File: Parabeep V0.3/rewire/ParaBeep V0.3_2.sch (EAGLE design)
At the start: 64 parts, among them IC2 MCP73811/2, Q1 500mA/300V, U1 ADXL345, U2 TPS78330DDCRDDC5_TEX-L, U3 TPS78330DDCRDDC5_TEX-L, U4 UBLOX_SAM_M8Q-0-10, U5 MS5803-14BA, U6 ATSAMD51J20A-A, U7 AT25SF128A-SHB-T, U8 RN4871-V/RM118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

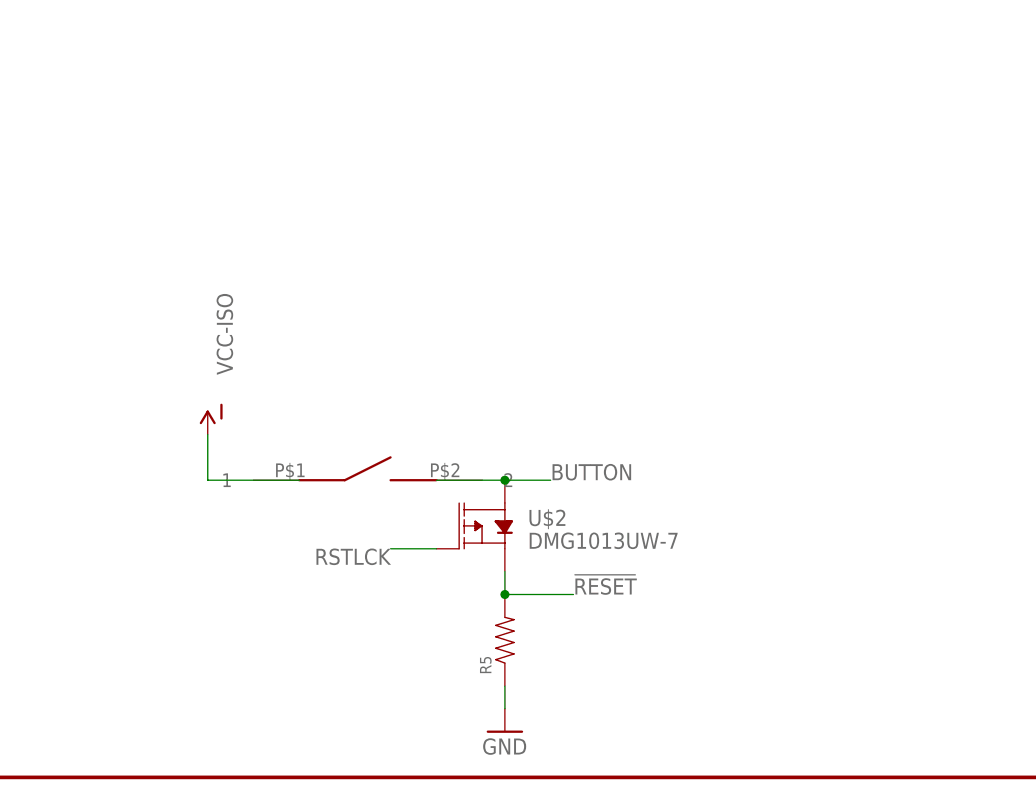
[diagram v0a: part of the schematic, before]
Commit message: bluetooth working, usb next
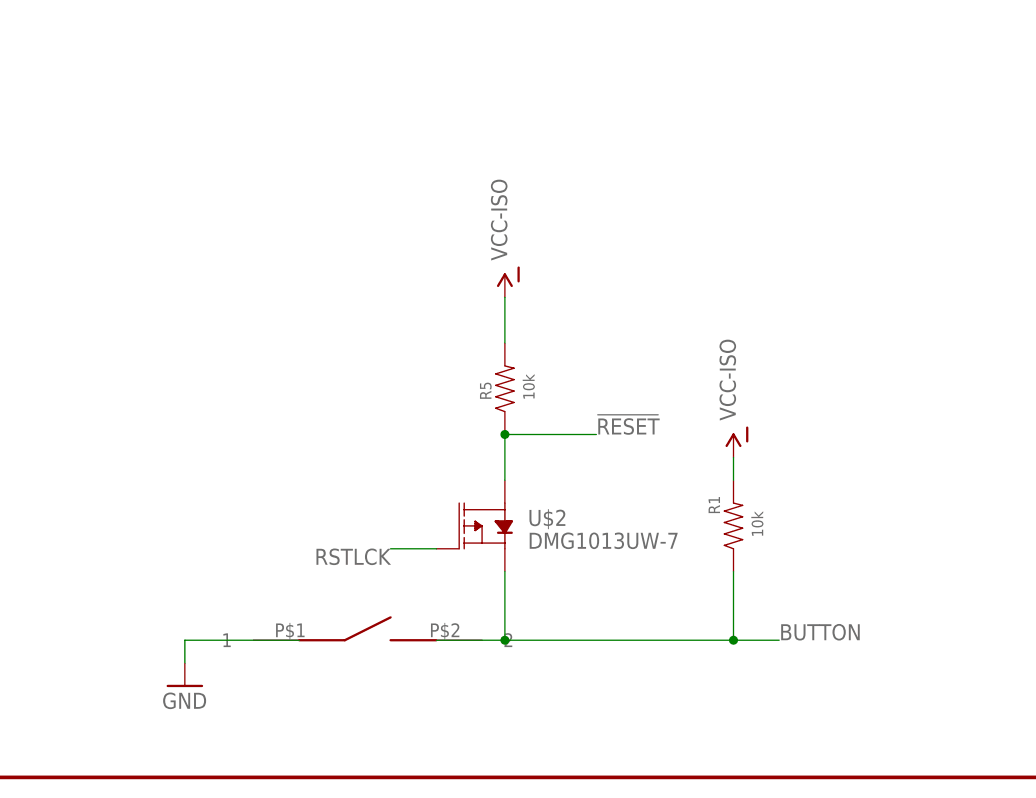
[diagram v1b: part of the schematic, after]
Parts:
- added R1: 10k, SparkFun-Resistors:RESISTOR0402
- R5: value (none) -> 10k
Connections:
- net !RESET: now also R5.1, U$2.S; no longer R5.2, U$2.D
- net BUTTON: now also R1.1, U$2.D; no longer U$2.S
- net GND: now also U$3.1; no longer R5.1
- net VCC-ISO: now also R1.2, R5.2; no longer U$3.1
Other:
- moved on the sheet: R5
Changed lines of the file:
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@@
 <part name="C12" library="SparkFun-Capacitors" deviceset="0.1UF" device="-0603-25V-(+80/-20%)" value="10uF"/>
 <part name="L2" library="SparkFun-Coils" deviceset="INDUCTOR" device="FB-30OHM"/>
-<part name="R5" library="SparkFun-Resistors" deviceset="RESISTOR" device="0402" value=" "/>
+<part name="R5" library="SparkFun-Resistors" deviceset="RESISTOR" device="0402" value="10k"/>
 <part name="GND4" library="SparkFun-Aesthetics" deviceset="GND" device=""/>
 <part name="SUPPLY10" library="SparkFun-PowerSymbols" deviceset="VCC_1" device=""/>
@@
 <part name="R12" library="SparkFun-Resistors" deviceset="RESISTOR" device="0402" value=" "/>
 <part name="GND23" library="SparkFun-Aesthetics" deviceset="GND" device=""/>
-<part name="U$6" library="SparkFun-PowerSymbols" deviceset="VCC-ISO" device=""/>
 <part name="J1" library="SparkFun-Connectors" deviceset="CONN_02" device="-JST-2MM-SMT"/>
 <part name="J3" library="SparkFun-Connectors" deviceset="CONN_02" device="-JST-2MM-SMT"/>
@@
 <part name="R6" library="SparkFun-Resistors" deviceset="RESISTOR" device="0402" value="100k"/>
 <part name="JP1" library="SparkFun-Jumpers" deviceset="JUMPER-SMT_3_1-NC_TRACE" device="_SILK" package3d_urn="urn:adsk.eagle:package:39288/1"/>
+<part name="U$6" library="SparkFun-PowerSymbols" deviceset="VCC-ISO" device=""/>
+<part name="R1" library="SparkFun-Resistors" deviceset="RESISTOR" device="0402" value="10k"/>
+<part name="U$8" library="SparkFun-PowerSymbols" deviceset="VCC-ISO" device=""/>
 </parts>
 <sheets>
@@
 <attribute name="VALUE" x="259.08" y="218.44" size="1.778" layer="96"/>
 </instance>
-<instance part="U$3" gate="G$1" x="254" y="33.02" smashed="yes"/>
+<instance part="U$3" gate="G$1" x="254" y="15.24" smashed="yes"/>
 <instance part="SUPPLY1" gate="G$1" x="25.4" y="259.08" smashed="yes">
 <attribute name="VALUE" x="25.4" y="261.874" size="1.778" layer="96" rot="MR0" align="bottom-center"/>
@@
 <attribute name="VALUE" x="73.66" y="184.15" size="1.778" layer="96" font="vector" rot="R90" align="top-left"/>
 </instance>
-<instance part="R5" gate="G$1" x="269.24" y="15.24" smashed="yes" rot="R90">
-<attribute name="NAME" x="267.7414" y="11.43" size="1.27" layer="95" rot="R90"/>
-<attribute name="VALUE" x="272.542" y="16.51" size="1.27" layer="96" rot="R90"/>
-</instance>
-<instance part="GND4" gate="1" x="269.24" y="5.08" smashed="yes">
-<attribute name="VALUE" x="266.7" y="2.54" size="1.778" layer="96"/>
+<instance part="R5" gate="G$1" x="269.24" y="43.18" smashed="yes" rot="R90">
+<attribute name="NAME" x="267.7414" y="41.91" size="1.27" layer="95" rot="R90"/>
+<attribute name="VALUE" x="272.542" y="41.91" size="1.27" layer="96" rot="R90"/>
+</instance>
+<instance part="GND4" gate="1" x="233.68" y="10.16" smashed="yes">
+<attribute name="VALUE" x="231.14" y="7.62" size="1.778" layer="96"/>
 </instance>
 <instance part="SUPPLY10" gate="G$2" x="248.92" y="259.08" smashed="yes">
@@
 <instance part="GND23" gate="1" x="190.5" y="22.86" smashed="yes">
 <attribute name="VALUE" x="193.04" y="22.86" size="1.778" layer="96"/>
-</instance>
-<instance part="U$6" gate="G$1" x="236.22" y="38.1" smashed="yes">
-<attribute name="VALUE" x="237.236" y="49.276" size="1.778" layer="96" rot="R270" align="bottom-center"/>
 </instance>
 <instance part="J1" gate="G$1" x="396.24" y="264.16" smashed="yes" rot="MR0">
@@
 </instance>
 <instance part="JP1" gate="G$1" x="381" y="259.08" smashed="yes" rot="R270"/>
+<instance part="U$6" gate="G$1" x="269.24" y="53.34" smashed="yes">
+<attribute name="VALUE" x="267.716" y="61.976" size="1.778" layer="96" rot="R270" align="bottom-center"/>
+</instance>
+<instance part="R1" gate="G$1" x="294.64" y="27.94" smashed="yes" rot="R90">
+<attribute name="NAME" x="293.1414" y="29.21" size="1.27" layer="95" rot="R90"/>
+<attribute name="VALUE" x="297.942" y="26.67" size="1.27" layer="96" rot="R90"/>
+</instance>
+<instance part="U$8" gate="G$1" x="294.64" y="35.56" smashed="yes">
+<attribute name="VALUE" x="293.116" y="44.196" size="1.778" layer="96" rot="R270" align="bottom-center"/>
+</instance>
 </instances>
 <busses>
@@
 <pinref part="Q1" gate="G$1" pin="E"/>
 <wire x1="60.96" y1="25.4" x2="60.96" y2="22.86" width="0.1524" layer="91"/>
-</segment>
-<segment>
-<pinref part="R5" gate="G$1" pin="1"/>
-<pinref part="GND4" gate="1" pin="GND"/>
-<wire x1="269.24" y1="7.62" x2="269.24" y2="10.16" width="0.1524" layer="91"/>
 </segment>
 <segment>
@@
 <pinref part="R3" gate="G$1" pin="1"/>
 </segment>
+<segment>
+<pinref part="U$3" gate="G$1" pin="1"/>
+<wire x1="246.38" y1="15.24" x2="233.68" y2="15.24" width="0.1524" layer="91"/>
+<pinref part="GND4" gate="1" pin="GND"/>
+<wire x1="233.68" y1="15.24" x2="233.68" y2="12.7" width="0.1524" layer="91"/>
+</segment>
 </net>
 <net name="CS_BARO" class="0">
@@
 </segment>
 <segment>
-<pinref part="U$2" gate="G$1" pin="D"/>
-<wire x1="269.24" y1="22.86" x2="269.24" y2="20.32" width="0.1524" layer="91"/>
-<label x="276.86" y="20.32" size="1.778" layer="95"/>
-<pinref part="R5" gate="G$1" pin="2"/>
-<wire x1="269.24" y1="20.32" x2="276.86" y2="20.32" width="0.1524" layer="91"/>
-<junction x="269.24" y="20.32"/>
-</segment>
-<segment>
 <pinref part="U6" gate="G$1" pin="!RESET"/>
 <wire x1="195.58" y1="182.88" x2="205.74" y2="182.88" width="0.1524" layer="91"/>
 <label x="198.12" y="182.88" size="1.778" layer="95"/>
+</segment>
+<segment>
+<pinref part="U$2" gate="G$1" pin="S"/>
+<pinref part="R5" gate="G$1" pin="1"/>
+<wire x1="269.24" y1="33.02" x2="269.24" y2="38.1" width="0.1524" layer="91"/>
+<wire x1="269.24" y1="38.1" x2="279.4" y2="38.1" width="0.1524" layer="91"/>
+<junction x="269.24" y="38.1"/>
+<label x="279.4" y="38.1" size="1.778" layer="95"/>
 </segment>
 </net>
@@
 </segment>
 <segment>
-<pinref part="U$3" gate="G$1" pin="1"/>
-<wire x1="246.38" y1="33.02" x2="236.22" y2="33.02" width="0.1524" layer="91"/>
-<wire x1="236.22" y1="33.02" x2="236.22" y2="38.1" width="0.1524" layer="91"/>
-<pinref part="U$6" gate="G$1" pin="VCC-ISO"/>
-</segment>
-<segment>
 <pinref part="JP3" gate="G$1" pin="VCC"/>
 <wire x1="345.44" y1="55.88" x2="340.36" y2="55.88" width="0.1524" layer="91" style="longdash"/>
@@
 <junction x="60.96" y="218.44"/>
 <pinref part="U$1" gate="G$1" pin="VCC-ISO"/>
+</segment>
+<segment>
+<pinref part="R5" gate="G$1" pin="2"/>
+<pinref part="U$6" gate="G$1" pin="VCC-ISO"/>
+<wire x1="269.24" y1="48.26" x2="269.24" y2="53.34" width="0.1524" layer="91"/>
+</segment>
+<segment>
+<pinref part="R1" gate="G$1" pin="2"/>
+<pinref part="U$8" gate="G$1" pin="VCC-ISO"/>
+<wire x1="294.64" y1="33.02" x2="294.64" y2="35.56" width="0.1524" layer="91"/>
 </segment>
 </net>
@@
 <wire x1="195.58" y1="114.3" x2="198.12" y2="114.3" width="0.1524" layer="91"/>
 <label x="198.12" y="114.3" size="1.778" layer="95"/>
-</segment>
-</net>
-<net name="BUTTON" class="0">
-<segment>
-<pinref part="U$3" gate="G$1" pin="2"/>
-<pinref part="U$2" gate="G$1" pin="S"/>
-<wire x1="261.62" y1="33.02" x2="269.24" y2="33.02" width="0.1524" layer="91"/>
-<wire x1="269.24" y1="33.02" x2="274.32" y2="33.02" width="0.1524" layer="91"/>
-<junction x="269.24" y="33.02"/>
-<label x="274.32" y="33.02" size="1.778" layer="95"/>
 </segment>
 </net>
@@
 </segment>
 </net>
+<net name="BUTTON" class="0">
+<segment>
+<pinref part="U$2" gate="G$1" pin="D"/>
+<wire x1="269.24" y1="22.86" x2="269.24" y2="15.24" width="0.1524" layer="91"/>
+<pinref part="U$3" gate="G$1" pin="2"/>
+<wire x1="269.24" y1="15.24" x2="261.62" y2="15.24" width="0.1524" layer="91"/>
+<wire x1="269.24" y1="15.24" x2="294.64" y2="15.24" width="0.1524" layer="91"/>
+<junction x="269.24" y="15.24"/>
+<wire x1="294.64" y1="15.24" x2="294.64" y2="22.86" width="0.1524" layer="91"/>
+<pinref part="R1" gate="G$1" pin="1"/>
+<wire x1="294.64" y1="15.24" x2="299.72" y2="15.24" width="0.1524" layer="91"/>
+<junction x="294.64" y="15.24"/>
+<label x="299.72" y="15.24" size="1.778" layer="95"/>
+</segment>
+</net>
